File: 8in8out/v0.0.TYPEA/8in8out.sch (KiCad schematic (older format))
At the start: 60 parts, among them IC1 ATTINY48-A, J1 RJ45, J2 RJ45, J3 CONN_6, K110 G5T-1-12VDC, K120 G5T-1-12VDC, K130 G5T-1-12VDC, K140 G5T-1-12VDC, K150 G5T-1-12VDC, K160 G5T-1-12VDC, K170 G5T-1-12VDC, K180 G5T-1-12VDC, P1 CONN_5, P100 CONN_2, P101 CONN_2, P102 CONN_2, P103 CONN_2, P105 CONN_2, P106 CONN_2, P110 CONN_2, P120 CONN_2, P130 CONN_2, P140 CONN_2, P150 CONN_2, P160 CONN_2, P170 CONN_2, P180 CONN_2, P2 CONN_5, P3 CONN_10X2, P4 CONN_2, U1 7805, U10 OPTO-TRANSISTOR, U2 ULN2803, U20 OPTO-TRANSISTOR, U30 OPTO-TRANSISTOR, U40 OPTO-TRANSISTOR, U50 OPTO-TRANSISTOR, U60 OPTO-TRANSISTOR, U70 OPTO-TRANSISTOR, U80 OPTO-TRANSISTOR

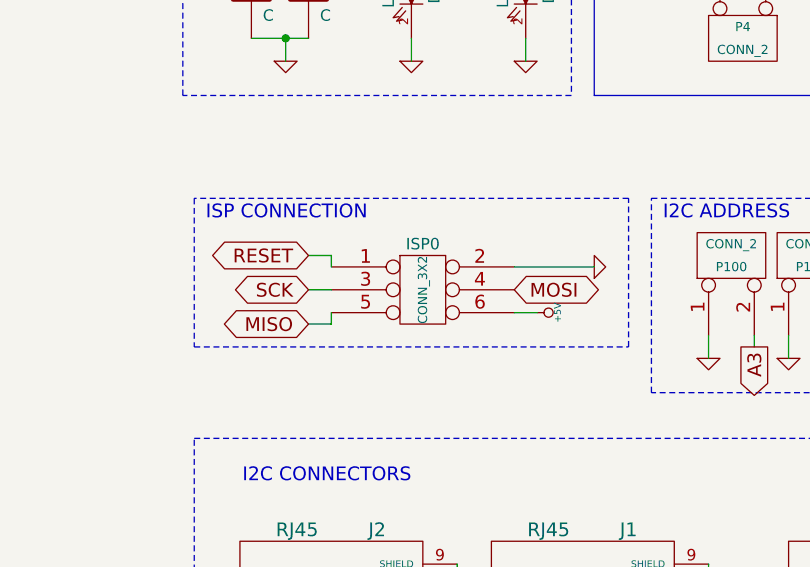
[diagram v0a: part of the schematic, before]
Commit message: correction connecteur ISP
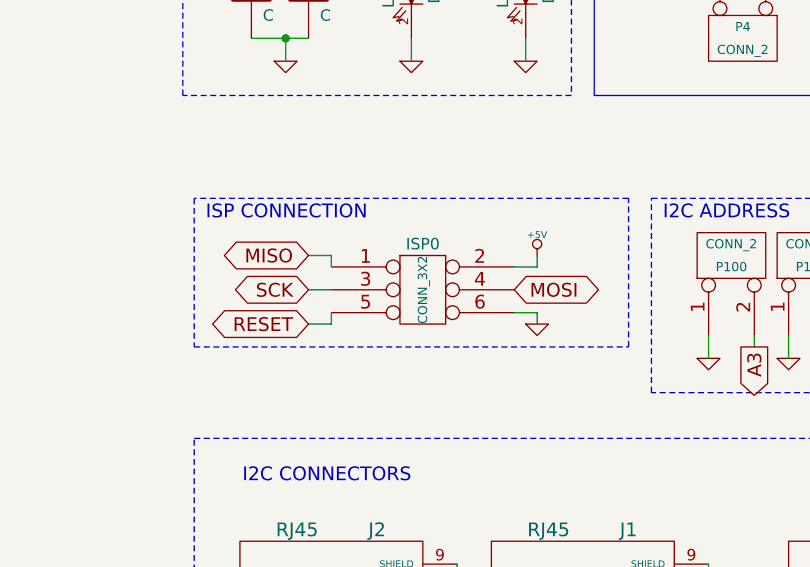
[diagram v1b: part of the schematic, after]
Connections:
- net +5V: now also ISP0.2; no longer ISP0.6
- net GND: now also ISP0.6; no longer ISP0.2
- net MISO: now also ISP0.1; no longer ISP0.5
- net RESET: now also ISP0.5; no longer ISP0.1
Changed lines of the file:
@@
-EESchema Schematic File Version 2  date sam. 27 avril 2013 16:03:43 CEST
+EESchema Schematic File Version 2
 LIBS:g5la-1-12vdc
 LIBS:power
@@
 LIBS:g5t-1-12vdc
 LIBS:8in8out-cache
-EELAYER 27 0
+EELAYER 24 0
 EELAYER END
 $Descr A2 23386 16535
@@
 L +5V #PWR03
 U 1 1 50670686
-P 11800 5050
-F 0 "#PWR03" H 11800 5140 20  0001 C CNN
-F 1 "+5V" H 11800 5140 30  0000 C CNN
-F 2 "" H 11800 5050 60  0001 C CNN
-F 3 "" H 11800 5050 60  0001 C CNN
-	1    11800 5050
-	0    1    1    0
+P 11800 4800
+F 0 "#PWR03" H 11800 4890 20  0001 C CNN
+F 1 "+5V" H 11800 4890 30  0000 C CNN
+F 2 "" H 11800 4800 60  0001 C CNN
+F 3 "" H 11800 4800 60  0001 C CNN
+	1    11800 4800
+	1    0    0    -1
 $EndComp
 Text Notes 10350 4650 0    60   ~ 0
@@
 L GND #PWR025
 U 1 1 5135D759
-P 12050 4850
-F 0 "#PWR025" H 12050 4850 30  0001 C CNN
-F 1 "GND" H 12050 4780 30  0001 C CNN
-F 2 "" H 12050 4850 60  0001 C CNN
-F 3 "" H 12050 4850 60  0001 C CNN
-	1    12050 4850
-	0    -1   -1   0
+P 11800 5100
+F 0 "#PWR025" H 11800 5100 30  0001 C CNN
+F 1 "GND" H 11800 5030 30  0001 C CNN
+F 2 "" H 11800 5100 60  0001 C CNN
+F 3 "" H 11800 5100 60  0001 C CNN
+	1    11800 5100
+	1    0    0    -1
 $EndComp
 $Comp
@@
 RESET
 Connection ~ 13700 10550
-Text GLabel 10800 4800 0    60   BiDi ~ 0
+Text GLabel 10800 5100 0    60   BiDi ~ 0
 RESET
 Text GLabel 10800 4950 0    60   BiDi ~ 0
 SCK
-Text GLabel 10800 5100 0    60   BiDi ~ 0
+Text GLabel 10800 4800 0    60   BiDi ~ 0
 MISO
 Text GLabel 11700 4950 2    60   BiDi ~ 0
@@
 Wire Wire Line
 	10900 5100 10900 5050
-Wire Wire Line
-	11700 4850 12050 4850
 $Comp
 L CONN_5 P1
@@
 	1    0    0    -1
 $EndComp
+Wire Wire Line
+	11800 5050 11800 5100
+Wire Wire Line
+	11700 4850 11800 4850
+Wire Wire Line
+	11800 4850 11800 4800
 $EndSCHEMATC
